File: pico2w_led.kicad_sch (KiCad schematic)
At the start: 16 parts, among them J1 Conn_01x20_MountingPin, J2 Conn_01x20_MountingPin, J3 Barrel_Jack, J4 Conn_01x04, U2 NTR3C21NZT3G, U3 NTR3C21NZT3G, U4 NTR3C21NZT3G, U5 AP62301WU-7

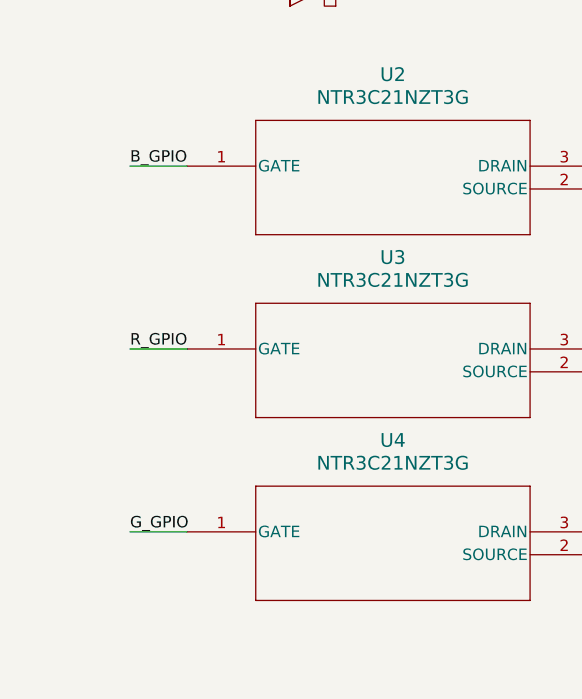
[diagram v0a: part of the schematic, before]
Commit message: add bleed resistors
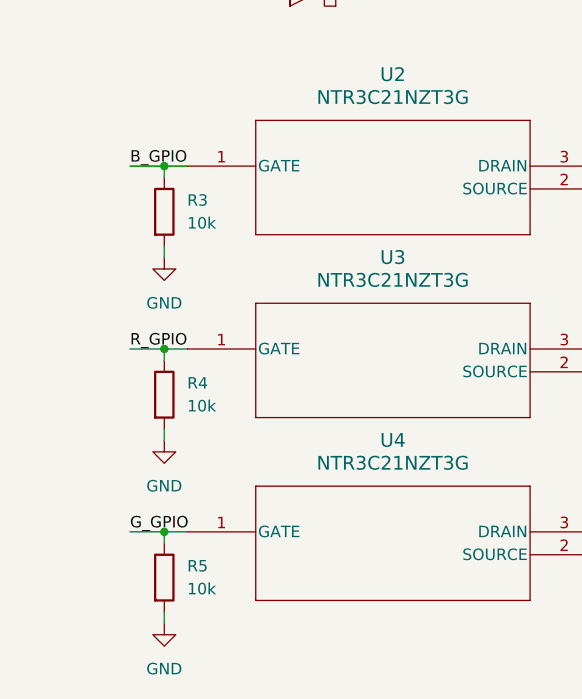
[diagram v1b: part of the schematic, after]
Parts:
- added R3, R4, R5: 10k, Resistor_SMD:R_1206_3216Metric, symbol Device:R
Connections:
- net B_GPIO: now also R3.1
- net GND: now also R3.2, R4.2, R5.2
- net GPIO_01: now also R5.1
- net GPIO_02: now also R4.1

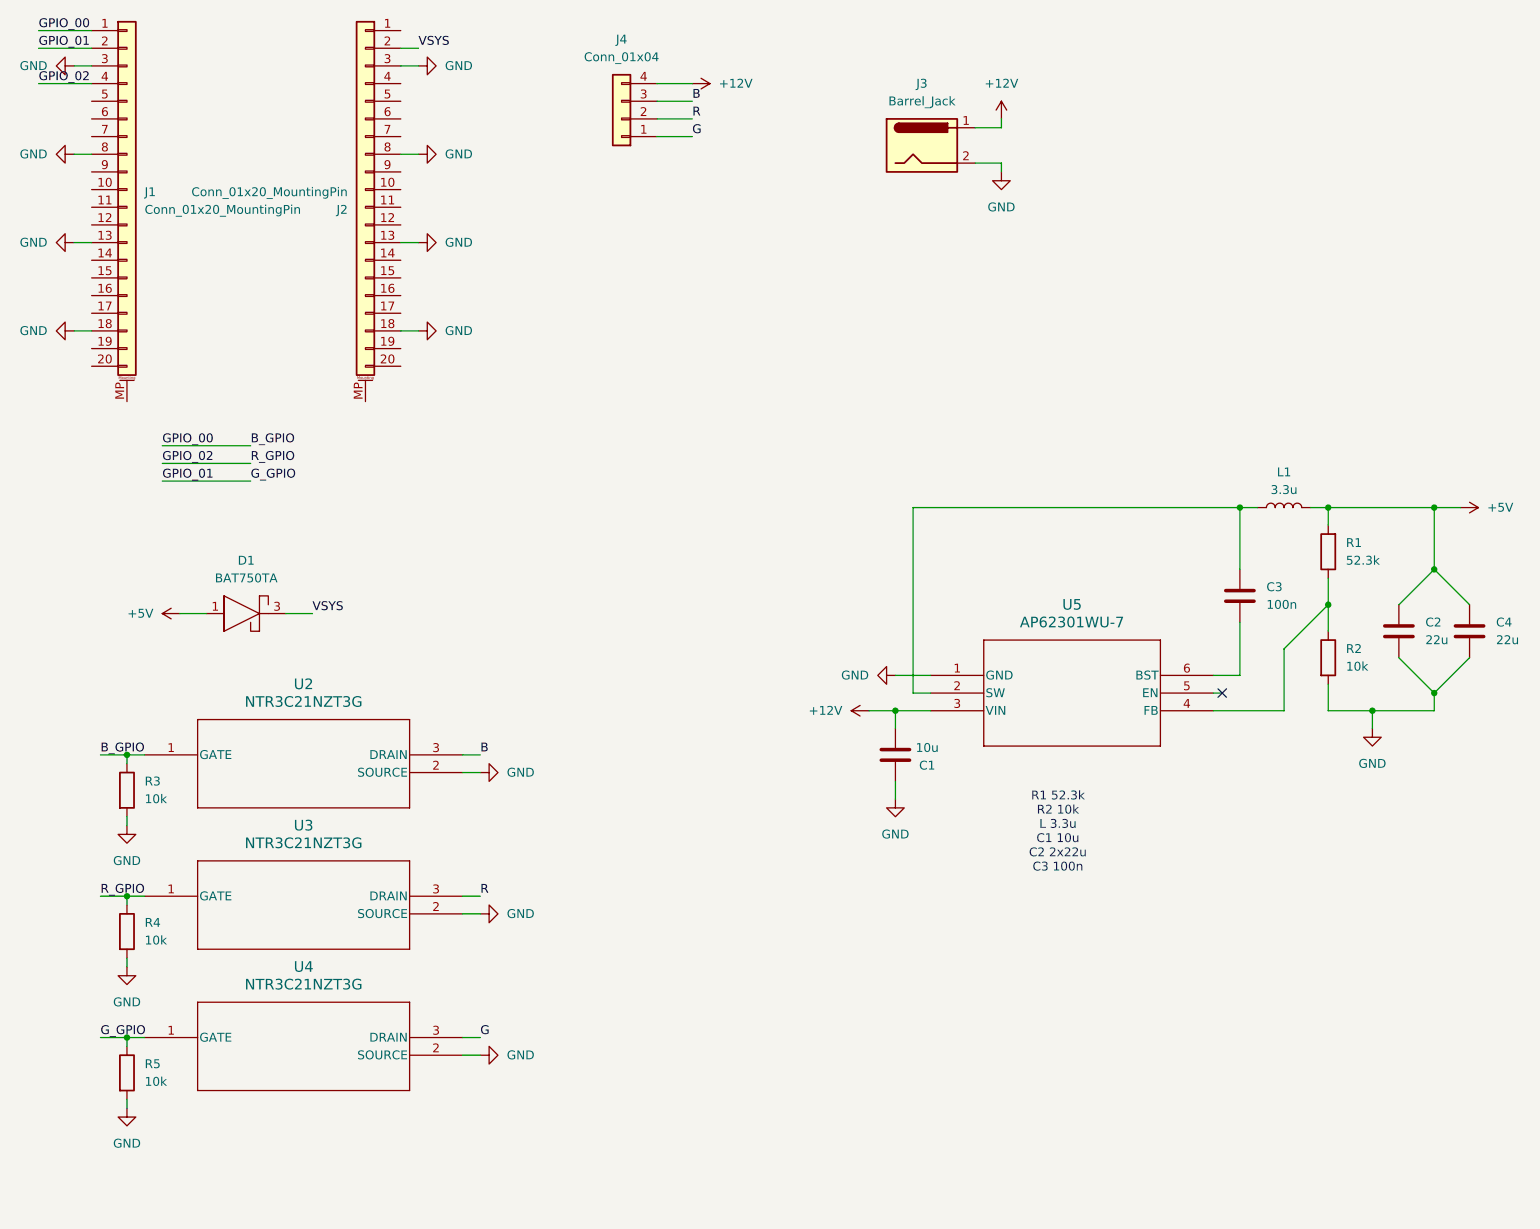
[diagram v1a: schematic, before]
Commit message: Add screw terminal
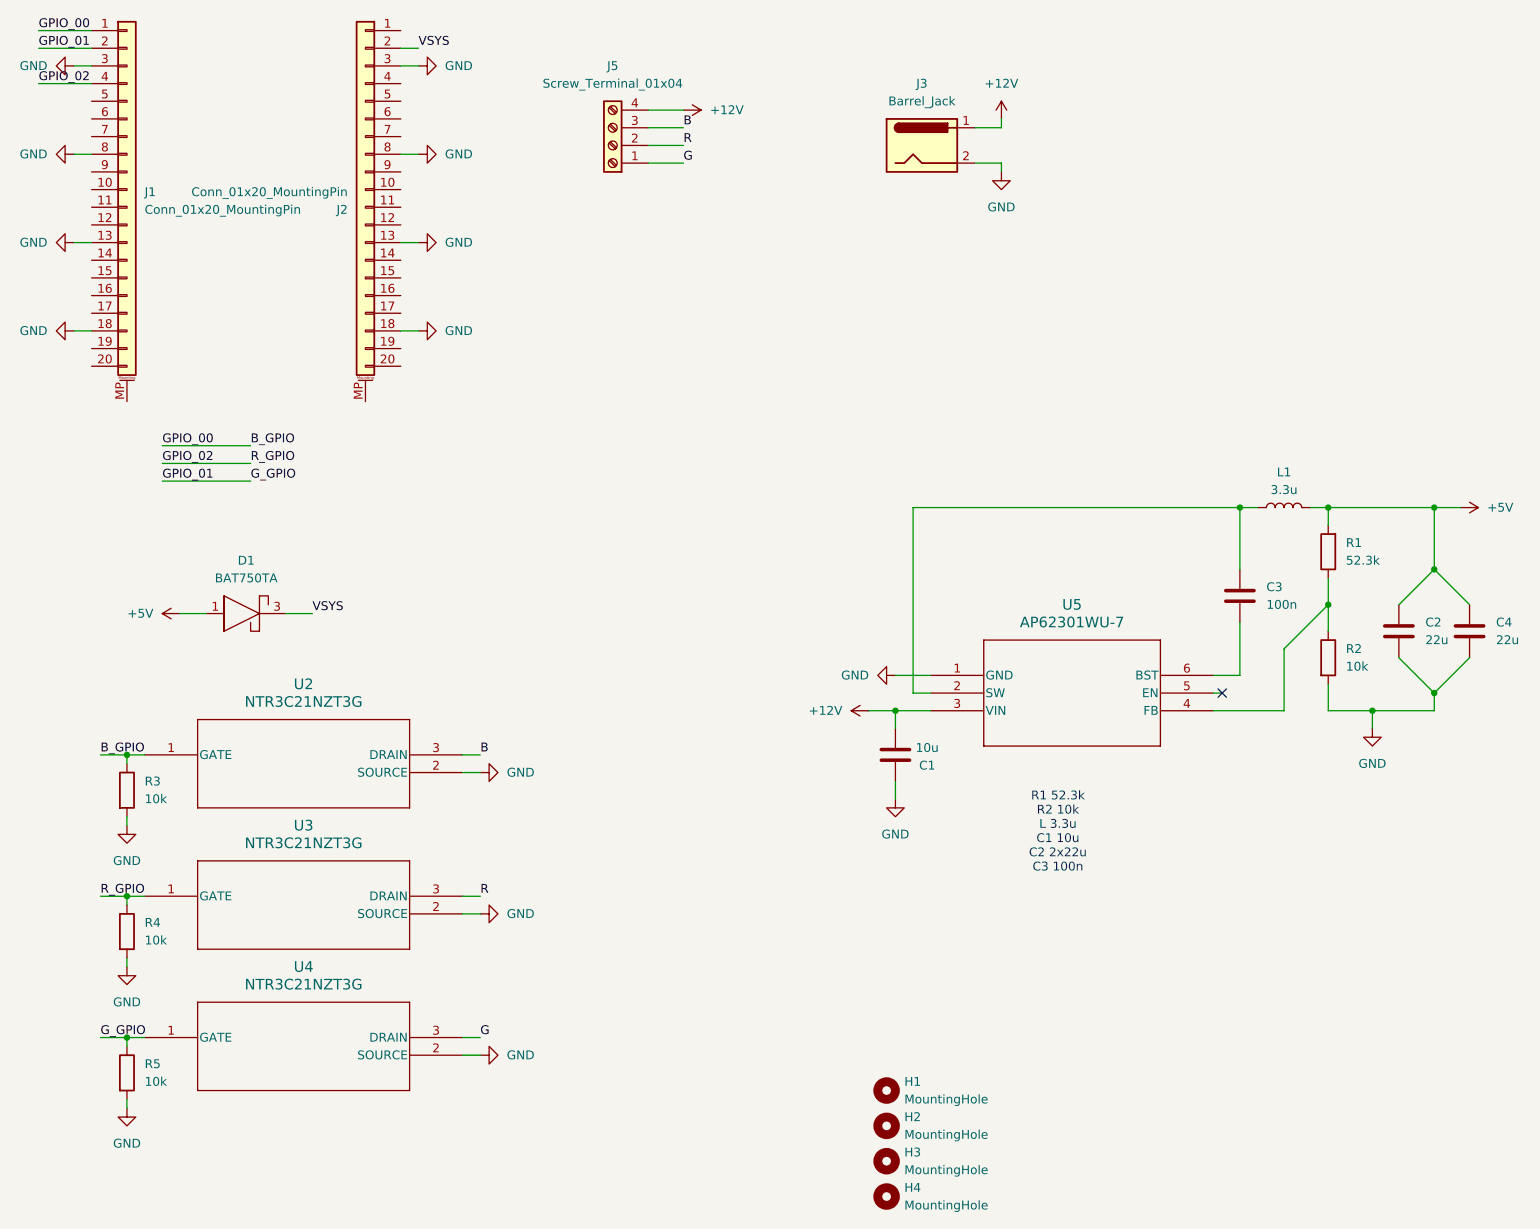
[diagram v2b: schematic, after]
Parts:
- removed J4: Conn_01x04, Connector_Wire:SolderWire-0.1sqmm_1x04_P3.6mm_D0.4mm_OD1mm, symbol Connector_Generic:Conn_01x04
- added H1, H2, H3, H4: MountingHole, MountingHole:MountingHole_2.2mm_M2, symbol Mechanical:MountingHole
- added J5: Screw_Terminal_01x04, NTR3C21NZT3G:TBD05-04-1-G-G, symbol Connector:Screw_Terminal_01x04
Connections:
- net +12V: now also J5.4 (Pin_4)
- net B: now also J5.3 (Pin_3)
- net G: now also J5.1 (Pin_1)
- net R: now also J5.2 (Pin_2)
